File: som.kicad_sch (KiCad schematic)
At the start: 38 parts, among them J10 5051101097, T2 BSS138APW, T4 BSS138APW, T5 BSS138APW

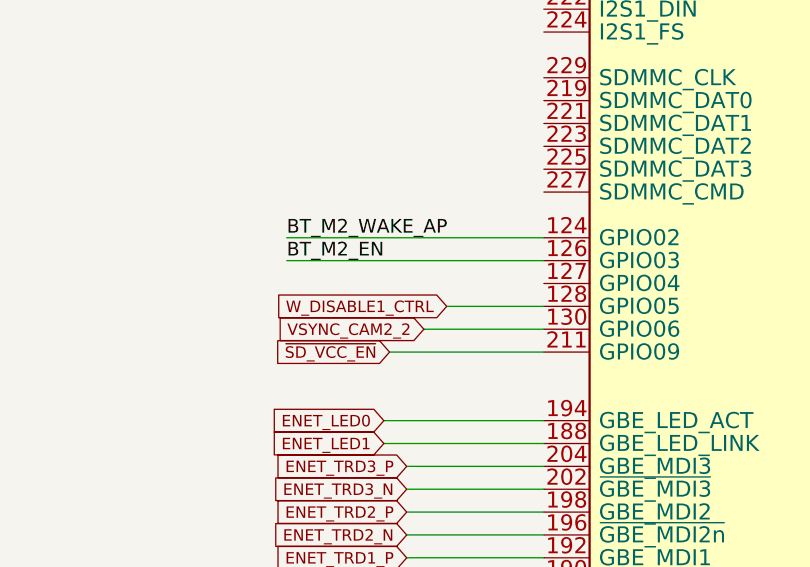
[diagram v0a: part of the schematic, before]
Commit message: Added possibility to reset I2C mux from SoM GPIO
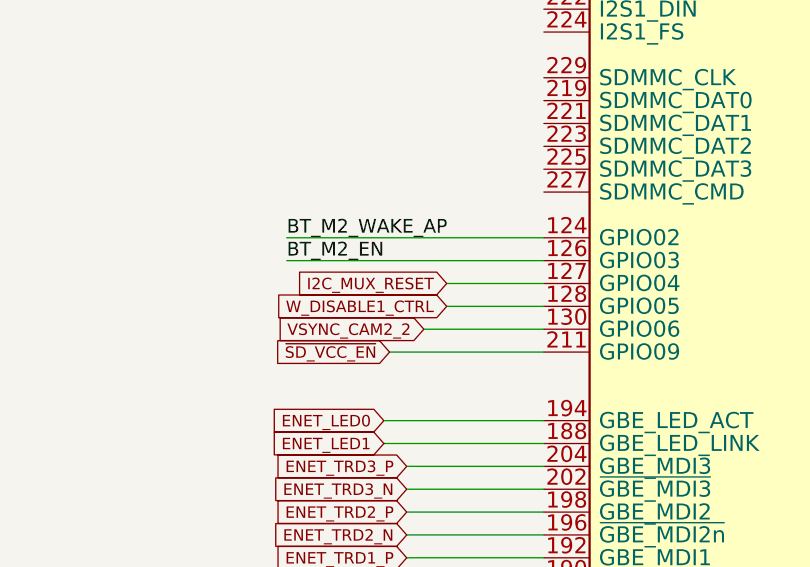
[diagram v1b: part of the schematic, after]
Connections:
- net I2C_MUX_RESET: now reaches M1.127 (GPIO04)
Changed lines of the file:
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@@
     (stroke (width 0) (type default) (color 0 0 0 0))
   )
+  (wire (pts (xy 106.045 217.805) (xy 116.84 217.805))
+    (stroke (width 0) (type default) (color 0 0 0 0))
+  )
   (wire (pts (xy 46.99 45.085) (xy 41.275 45.085))
     (stroke (width 0) (type default) (color 0 0 0 0))
@@
     )
   )
+  (global_label "I2C_MUX_RESET" (shape input) (at 106.045 217.805 180) (fields_autoplaced)
+    (effects (font (size 1.27 1.27)) (justify right))
+    (property "Intersheet References" "${INTERSHEET_REFS}" (id 0) (at 88.9646 217.7256 0)
+      (effects (font (size 1.27 1.27)) (justify right) hide)
+    )
+  )

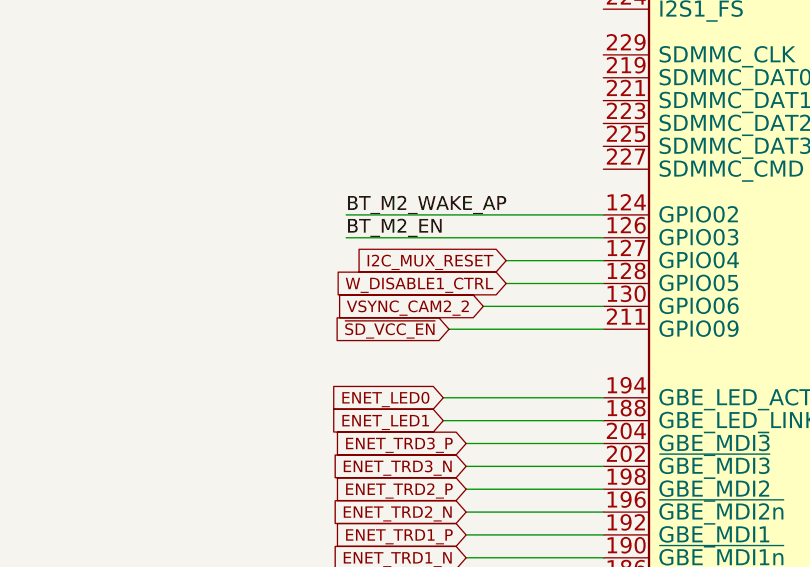
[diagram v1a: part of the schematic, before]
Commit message: Added USB OTG functionality
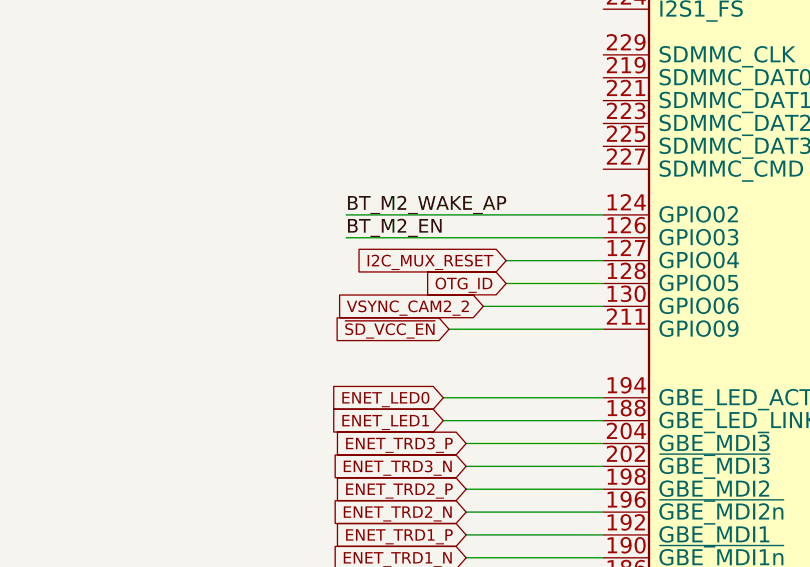
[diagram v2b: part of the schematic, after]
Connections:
- net W_DISABLE1_CTRL renamed OTG_ID
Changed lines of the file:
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@@
-    )
-  )
-  (global_label "W_DISABLE1_CTRL" (shape input) (at 106.045 220.345 180) (fields_autoplaced)
-    (effects (font (size 1.27 1.27)) (justify right))
-    (property "Intersheet References" "${INTERSHEET_REFS}" (id 0) (at 0 0 0)
-      (effects (font (size 1.27 1.27)) hide)
     )
   )
@@
     )
   )
+  (global_label "OTG_ID" (shape input) (at 106.045 220.345 180) (fields_autoplaced)
+    (effects (font (size 1.27 1.27)) (justify right))
+    (property "Intersheet References" "${INTERSHEET_REFS}" (id 0) (at 97.3103 220.2656 0)
+      (effects (font (size 1.27 1.27)) (justify right) hide)
+    )
+  )

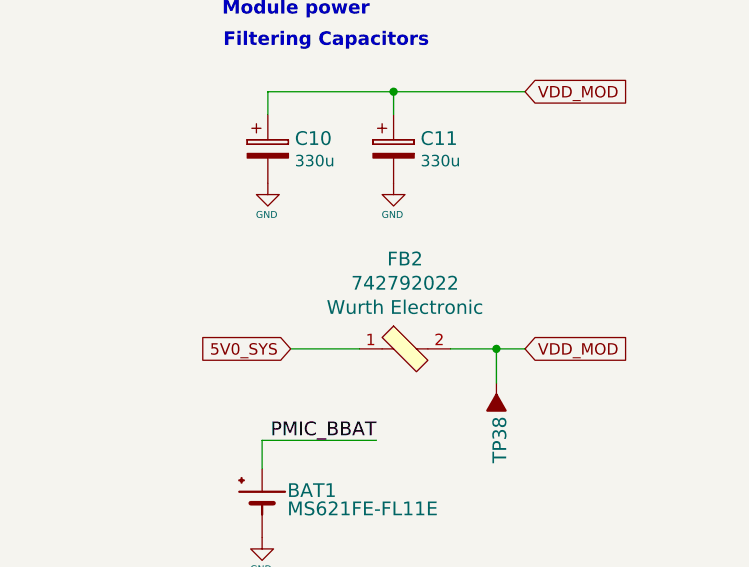
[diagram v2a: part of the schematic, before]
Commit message: Replaced 742792022 ferrites with 74279220181 for higher current capability
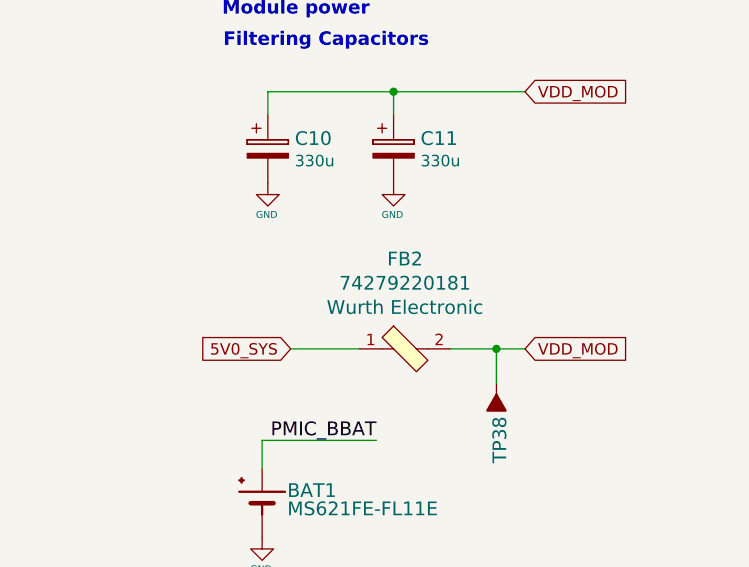
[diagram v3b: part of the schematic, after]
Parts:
- FB2: value 742792022 -> 74279220181; symbol jetson-nano-baseboard:742792022 -> jetson-nano-baseboard:74279220181; MPN 742792022 -> 74279220181
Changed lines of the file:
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@@
     (pin "2")
   )
-  (symbol (lib_id "jetson-nano-baseboard:742792022") (at 365.76 61.595 0) (unit 1)
+  (symbol (lib_id "jetson-nano-baseboard:74279220181") (at 365.76 61.595 0) (unit 1)
     (in_bom yes) (on_board yes)
     (property "Reference" "FB2" (id 0) (at 365.76 51.6128 0)
       (effects (font (size 1.524 1.524)))
     )
-    (property "Value" "742792022" (id 1) (at 365.76 56.9976 0)
+    (property "Value" "74279220181" (id 1) (at 365.76 56.9976 0)
       (effects (font (size 1.524 1.524)) hide)
     )
@@
       (effects (font (size 1.524 1.524)) (justify left) hide)
     )
-    (property "Datasheet" "https://www.we-online.com/katalog/datasheet/742792022.pdf" (id 3) (at 370.84 53.975 0)
+    (property "Datasheet" "https://www.we-online.com/components/products/datasheet/74279220181.pdf" (id 3) (at 370.84 53.975 0)
       (effects (font (size 1.524 1.524)) (justify left) hide)
     )
-    (property "MPN" "742792022" (id 4) (at 365.76 54.3052 0)
+    (property "MPN" "74279220181" (id 4) (at 365.76 54.3052 0)
       (effects (font (size 1.524 1.524)))
     )

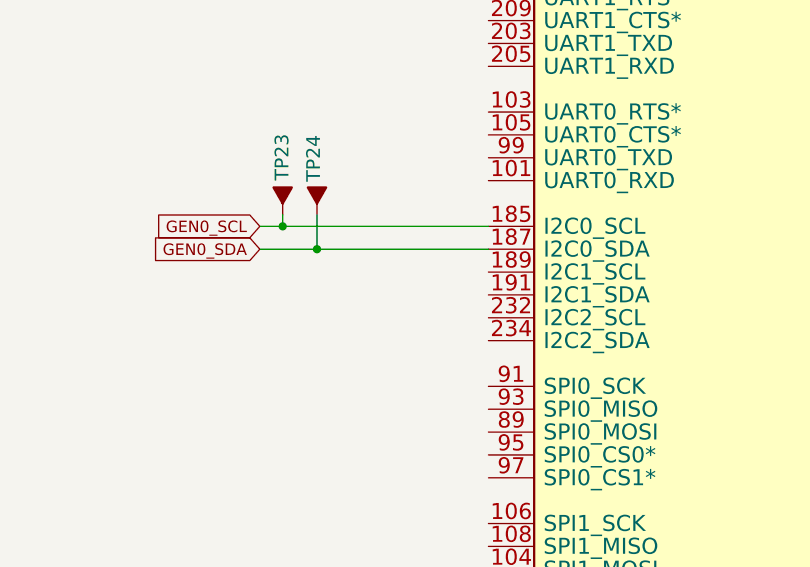
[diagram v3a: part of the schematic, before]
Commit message: Added I2C connector
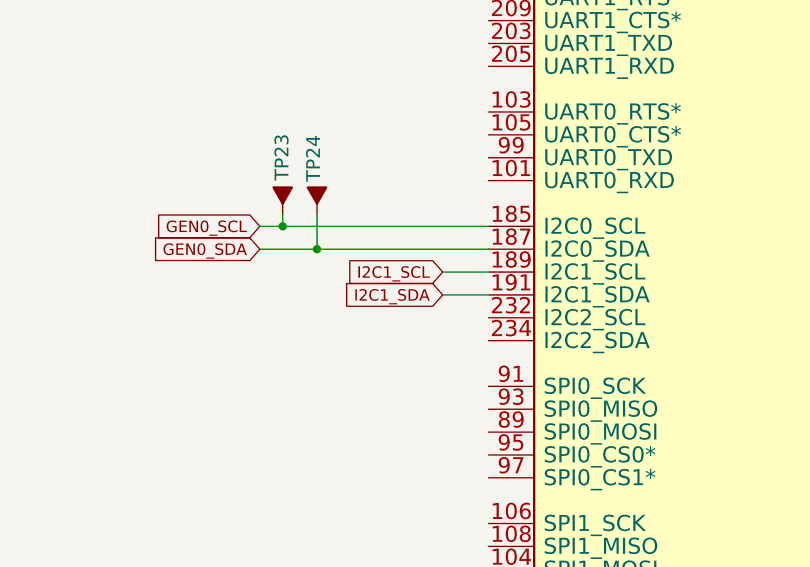
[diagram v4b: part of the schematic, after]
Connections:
- net I2C1_SCL: now reaches M1.189 (I2C1_SCL)
- net I2C1_SDA: now reaches M1.191 (I2C1_SDA)
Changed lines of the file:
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@@
     (stroke (width 0) (type default) (color 0 0 0 0))
   )
+  (wire (pts (xy 201.295 75.565) (xy 206.375 75.565))
+    (stroke (width 0) (type default) (color 0 0 0 0))
+  )
   (wire (pts (xy 97.79 60.325) (xy 99.695 60.325))
     (stroke (width 0) (type default) (color 0 0 0 0))
@@
     (stroke (width 0) (type default) (color 0 0 0 0))
   )
+  (wire (pts (xy 201.295 73.025) (xy 206.375 73.025))
+    (stroke (width 0) (type default) (color 0 0 0 0))
+  )
   (wire (pts (xy 116.84 235.585) (xy 99.06 235.585))
     (stroke (width 0) (type default) (color 0 0 0 0))
@@
     )
   )
+  (global_label "I2C1_SDA" (shape input) (at 201.295 75.565 180) (fields_autoplaced)
+    (effects (font (size 1.27 1.27)) (justify right))
+    (property "Intersheet References" "${INTERSHEET_REFS}" (id 0) (at 190.1413 75.4856 0)
+      (effects (font (size 1.27 1.27)) (justify right) hide)
+    )
+  )
   (global_label "OTG_USB_D_P" (shape input) (at 198.12 136.525 180) (fields_autoplaced)
     (effects (font (size 1.27 1.27)) (justify right))
@@
     )
   )
+  (global_label "I2C1_SCL" (shape input) (at 201.295 73.025 180) (fields_autoplaced)
+    (effects (font (size 1.27 1.27)) (justify right))
+    (property "Intersheet References" "${INTERSHEET_REFS}" (id 0) (at 190.2018 72.9456 0)
+      (effects (font (size 1.27 1.27)) (justify right) hide)
+    )
+  )

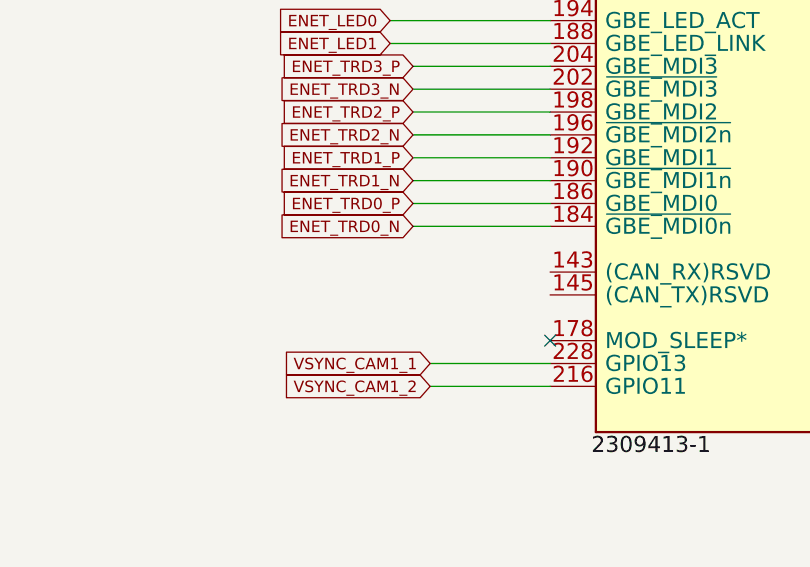
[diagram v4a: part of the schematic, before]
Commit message: Added CAN interface
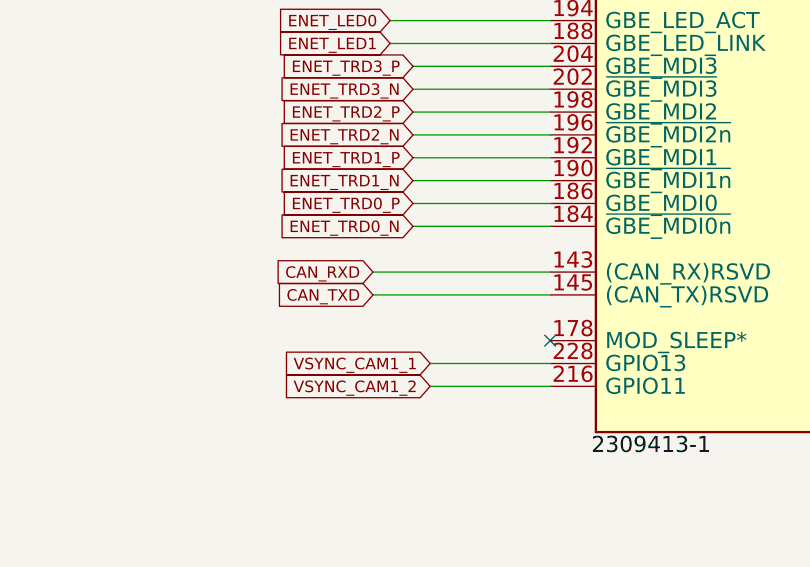
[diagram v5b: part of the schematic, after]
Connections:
- net CAN_RXD: now reaches M1.143 ((CAN_RX)RSVD)
- net CAN_TXD: now reaches M1.145 ((CAN_TX)RSVD)
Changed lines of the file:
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@@
     (stroke (width 0) (type default) (color 0 0 0 0))
   )
+  (wire (pts (xy 97.155 260.985) (xy 116.84 260.985))
+    (stroke (width 0) (type default) (color 0 0 0 0))
+  )
   (wire (pts (xy 46.99 108.585) (xy 43.815 108.585))
     (stroke (width 0) (type default) (color 0 0 0 0))
@@
     (stroke (width 0) (type default) (color 0 0 0 0))
   )
+  (wire (pts (xy 97.155 263.525) (xy 116.84 263.525))
+    (stroke (width 0) (type default) (color 0 0 0 0))
+  )
   (wire (pts (xy 205.74 186.055) (xy 192.405 186.055))
     (stroke (width 0) (type default) (color 0 0 0 0))
@@
     )
   )
+  (global_label "CAN_TXD" (shape input) (at 97.155 263.525 180) (fields_autoplaced)
+    (effects (font (size 1.27 1.27)) (justify right))
+    (property "Intersheet References" "${INTERSHEET_REFS}" (id 0) (at 86.727 263.4456 0)
+      (effects (font (size 1.27 1.27)) (justify right) hide)
+    )
+  )
   (global_label "PCIE1_RST" (shape input) (at 188.595 183.515 180) (fields_autoplaced)
     (effects (font (size 1.27 1.27)) (justify right))
@@
     )
   )
+  (global_label "CAN_RXD" (shape input) (at 97.155 260.985 180) (fields_autoplaced)
+    (effects (font (size 1.27 1.27)) (justify right))
+    (property "Intersheet References" "${INTERSHEET_REFS}" (id 0) (at 86.4246 260.9056 0)
+      (effects (font (size 1.27 1.27)) (justify right) hide)
+    )
+  )

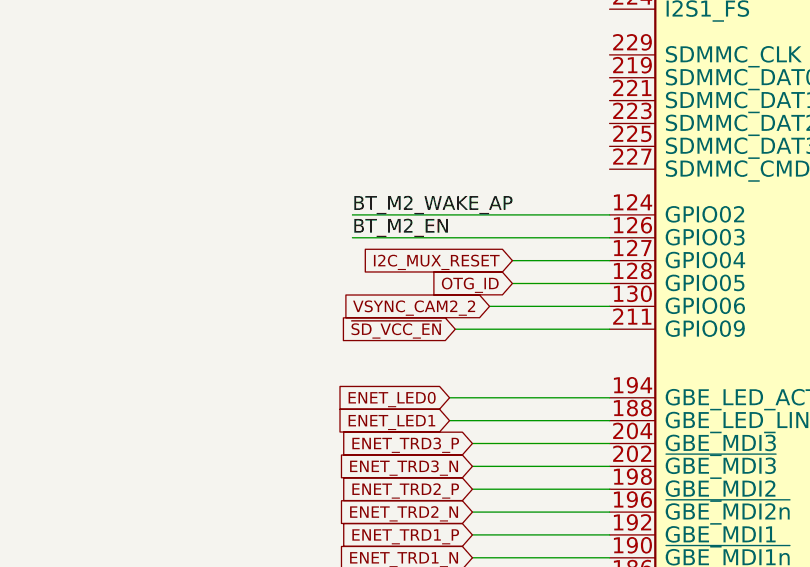
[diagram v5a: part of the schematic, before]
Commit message: Resolve TOOD on USB sheet
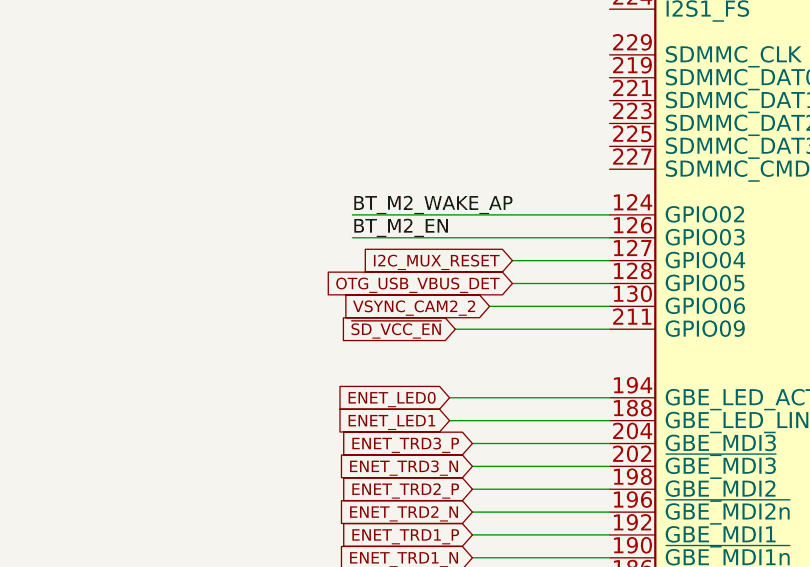
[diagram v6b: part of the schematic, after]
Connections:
- net OTG_ID renamed OTG_USB_VBUS_DET
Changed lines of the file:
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@@
-    )
-  )
-  (global_label "OTG_ID" (shape input) (at 106.045 220.345 180) (fields_autoplaced)
-    (effects (font (size 1.27 1.27)) (justify right))
-    (property "Intersheet References" "${INTERSHEET_REFS}" (id 0) (at 97.3103 220.2656 0)
-      (effects (font (size 1.27 1.27)) (justify right) hide)
     )
   )
@@
     )
   )
+  (global_label "OTG_USB_VBUS_DET" (shape input) (at 106.045 220.345 180) (fields_autoplaced)
+    (effects (font (size 1.27 1.27)) (justify right))
+    (property "Intersheet References" "${INTERSHEET_REFS}" (id 0) (at 85.1546 220.2656 0)
+      (effects (font (size 1.27 1.27)) (justify right) hide)
+    )
+  )

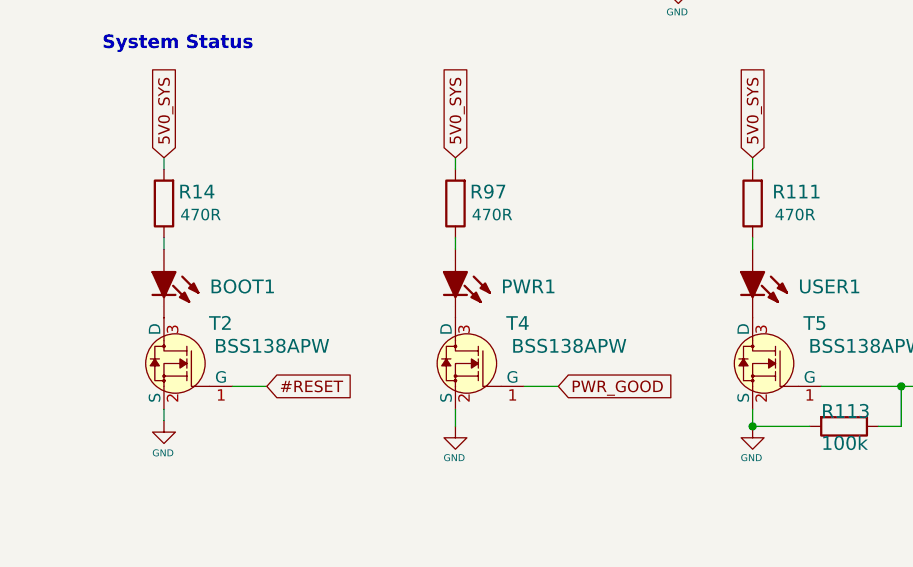
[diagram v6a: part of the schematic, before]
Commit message: Continue placement, mix USB SS signals as HD3SS3220 allows for it
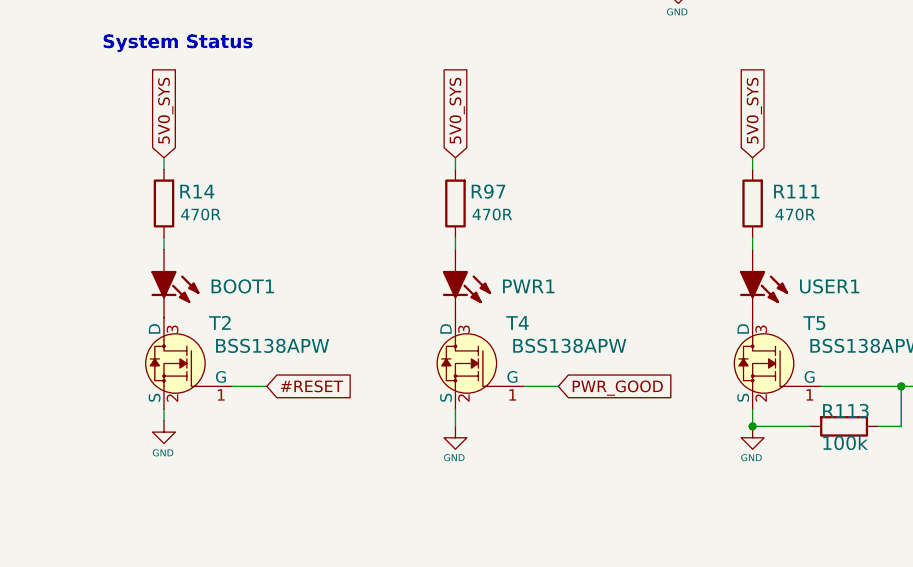
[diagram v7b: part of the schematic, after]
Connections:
- net at R111.1: now also USER1.1 (A); no longer USER1.A
- net at T5.3 (D): now also USER1.2 (K); no longer USER1.K
- net at R97.1: now also PWR1.1 (A); no longer PWR1.A
- net at T4.3 (D): now also PWR1.2 (K); no longer PWR1.K
- net at R14.1: now also BOOT1.1 (A); no longer BOOT1.A
- net at T2.3 (D): now also BOOT1.2 (K); no longer BOOT1.K
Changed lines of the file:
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@@
     (pin "2")
   )
-  (symbol (lib_id "jetson-nano-baseboard:LED") (at 358.14 114.935 270) (unit 1)
+  (symbol (lib_name "LED_2") (lib_id "jetson-nano-baseboard:LED") (at 358.14 114.935 270) (unit 1)
     (in_bom yes) (on_board yes)
     (property "Reference" "USER1" (id 0) (at 363.22 117.475 90)
@@
       (effects (font (size 1.27 1.27)) hide)
     )
-    (pin "A")
-    (pin "K")
+    (pin "1")
+    (pin "2")
   )
   (symbol (lib_id "jetson-nano-baseboard:Jetson-Nano-new-release") (at 109.22 188.595 0) (unit 7)
@@
     (pin "1")
   )
-  (symbol (lib_id "jetson-nano-baseboard:LED") (at 325.12 114.935 270) (unit 1)
+  (symbol (lib_name "LED_1") (lib_id "jetson-nano-baseboard:LED") (at 325.12 114.935 270) (unit 1)
     (in_bom yes) (on_board yes)
     (property "Reference" "PWR1" (id 0) (at 330.2 117.475 90)
@@
       (effects (font (size 1.27 1.27)) hide)
     )
-    (pin "A")
-    (pin "K")
+    (pin "1")
+    (pin "2")
   )
   (symbol (lib_id "jetson-nano-baseboard:LED") (at 292.735 114.935 270) (unit 1)
@@
       (effects (font (size 1.27 1.27)) hide)
     )
-    (pin "A")
-    (pin "K")
+    (pin "1")
+    (pin "2")
   )
   (symbol (lib_id "jetson-nano-baseboard:TL3340AF160QG") (at 295.275 184.785 0) (unit 1)
